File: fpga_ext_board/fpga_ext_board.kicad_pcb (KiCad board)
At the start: 2 copper layers, 100 x 100 mm, 3 parts

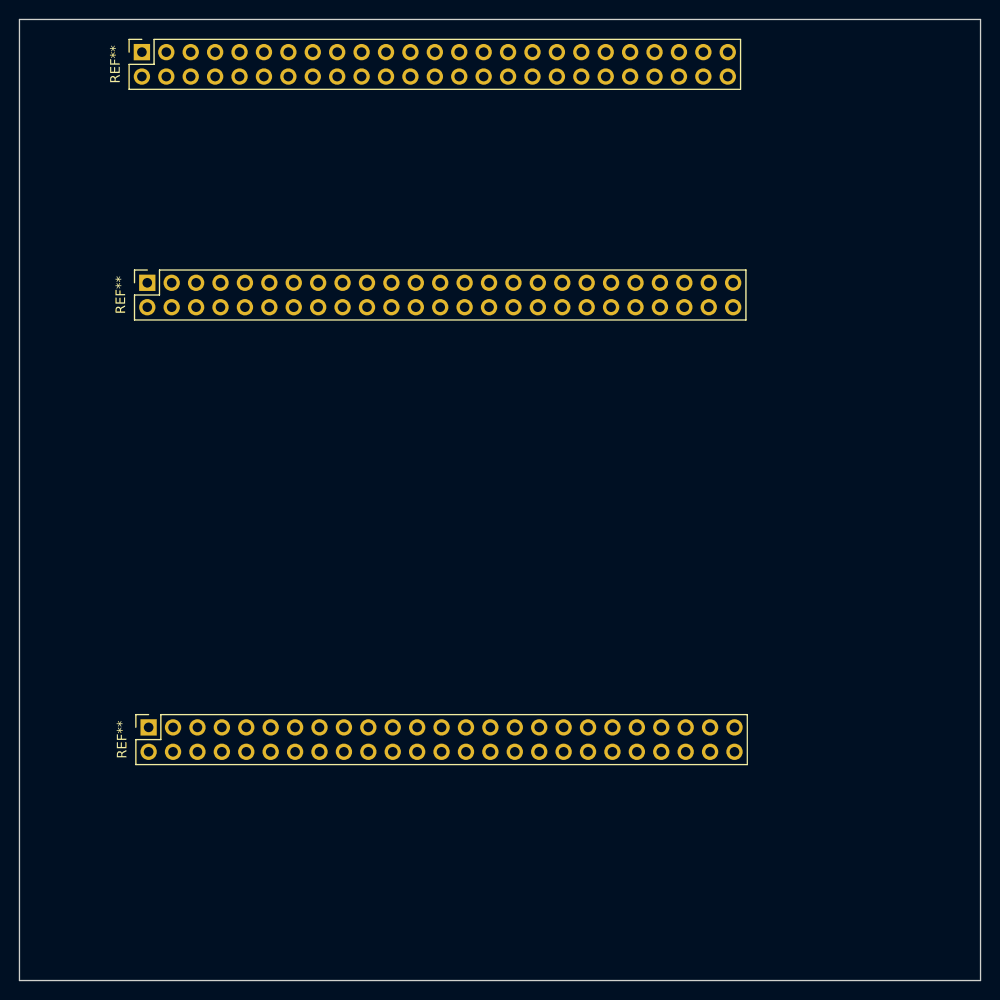
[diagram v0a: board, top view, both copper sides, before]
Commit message: add initial version of holder
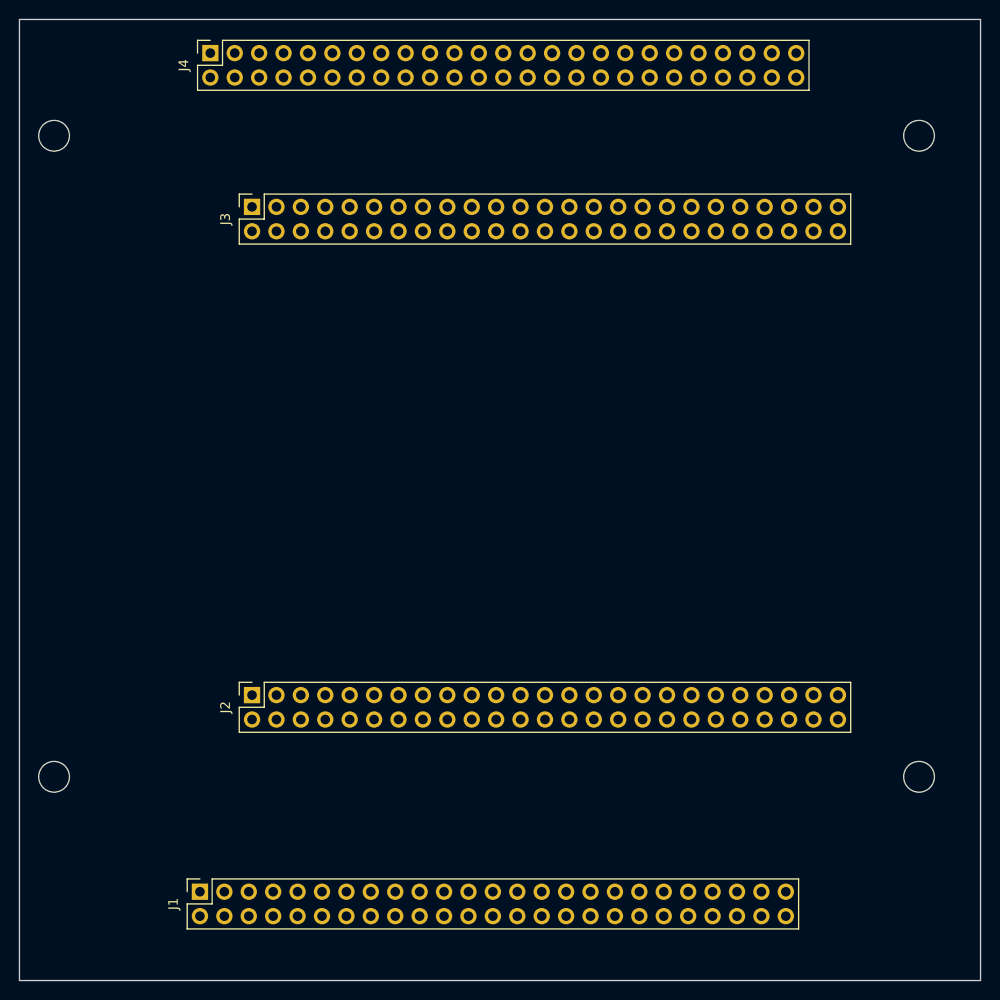
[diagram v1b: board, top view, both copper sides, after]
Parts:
- removed REF** (x3): PinSocket_2x25_P2.54mm_Vertical, Connector_PinSocket_2.54mm:PinSocket_2x25_P2.54mm_Vertical
- added J1: Conn_02x25_Odd_Even, Connector_PinSocket_2.54mm:PinSocket_2x25_P2.54mm_Vertical, F.Cu at (75.5, 141.8)
- added J2: Conn_02x25_Odd_Even, Connector_PinSocket_2.54mm:PinSocket_2x25_P2.54mm_Vertical, F.Cu at (80.9, 121.3)
- added J3: Conn_02x25_Odd_Even, Connector_PinSocket_2.54mm:PinSocket_2x25_P2.54mm_Vertical, F.Cu at (80.9, 70.5)
- added J4: Conn_02x25_Odd_Even, Connector_PinSocket_2.54mm:PinSocket_2x25_P2.54mm_Vertical, F.Cu at (76.6, 54.5)
- added REF1: MountingHole_3.2mm_M3, MountingHole:MountingHole_3.2mm_M3, F.Cu at (60.3, 63.1)
- added REF2: MountingHole_3.2mm_M3, MountingHole:MountingHole_3.2mm_M3, F.Cu at (150.3, 63.1)
- added REF3: MountingHole_3.2mm_M3, MountingHole:MountingHole_3.2mm_M3, F.Cu at (60.3, 129.8)
- added REF4: MountingHole_3.2mm_M3, MountingHole:MountingHole_3.2mm_M3, F.Cu at (150.3, 129.8)
